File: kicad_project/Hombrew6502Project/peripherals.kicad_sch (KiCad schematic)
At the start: 15 parts, among them J401 SD CARD, J402 Micro_SD_Card, U401 74HCT125D, U402 M95512-Axxx-MF

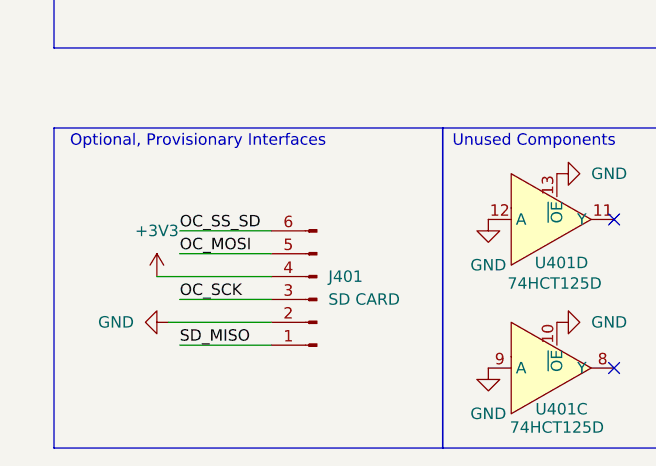
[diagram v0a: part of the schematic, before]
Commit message: footprint assignments and separate project for RAM board
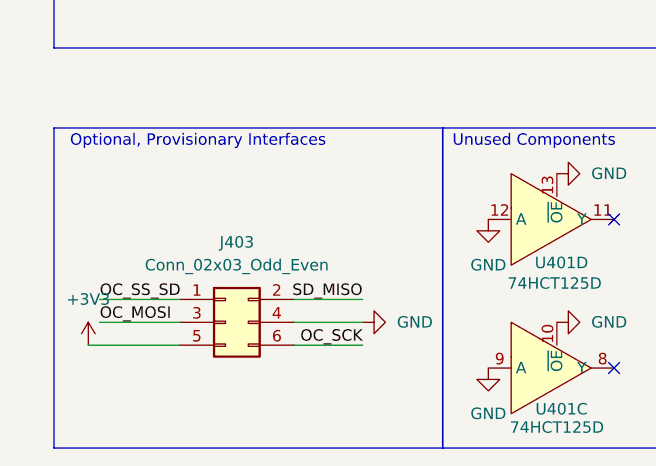
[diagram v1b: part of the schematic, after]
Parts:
- removed J401: SD CARD, symbol Connector:Conn_01x06_Pin
- added J403: Conn_02x03_Odd_Even, Connector_PinHeader_2.54mm:PinHeader_2x03_P2.54mm_Vertical_SMD, symbol Connector_Generic:Conn_02x03_Odd_Even
- J402: footprint (none) -> Connector_Card:microSD_HC_Wuerth_693072010801
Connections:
- net +3V3: now also J403.5 (Pin_5)
- net GND: now also J403.4 (Pin_4)
- net OC_MOSI: now also J403.3 (Pin_3)
- net OC_SCK: now also J403.6 (Pin_6)
- net OC_SS_SD: now also J403.1 (Pin_1)
- net SD_MISO: now also J403.2 (Pin_2)
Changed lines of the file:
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@@
 	(wire
 		(pts
-			(xy 35.56 173.99) (xy 45.72 173.99)
+			(xy 55.88 179.07) (xy 48.26 179.07)
 		)
 		(stroke
@@
 	(wire
 		(pts
-			(xy 33.02 171.45) (xy 45.72 171.45)
+			(xy 25.4 179.07) (xy 35.56 179.07)
 		)
 		(stroke
@@
 	(wire
 		(pts
-			(xy 34.29 176.53) (xy 45.72 176.53)
+			(xy 55.88 176.53) (xy 48.26 176.53)
 		)
 		(stroke
@@
 	(wire
 		(pts
-			(xy 35.56 166.37) (xy 45.72 166.37)
+			(xy 26.67 173.99) (xy 35.56 173.99)
 		)
 		(stroke
@@
 	(wire
 		(pts
-			(xy 35.56 179.07) (xy 45.72 179.07)
+			(xy 55.88 173.99) (xy 48.26 173.99)
 		)
 		(stroke
@@
 	(wire
 		(pts
-			(xy 35.56 168.91) (xy 45.72 168.91)
+			(xy 26.67 176.53) (xy 35.56 176.53)
 		)
 		(stroke
@@
 	)
 	(label "OC_SCK"
-		(at 35.56 173.99 0)
+		(at 55.88 179.07 180)
 		(effects
 			(font
 				(size 1.27 1.27)
 			)
-			(justify left bottom)
+			(justify right bottom)
 		)
 	)
 	(label "SD_MISO"
-		(at 35.56 179.07 0)
+		(at 55.88 173.99 180)
 		(effects
 			(font
 				(size 1.27 1.27)
 			)
-			(justify left bottom)
+			(justify right bottom)
 		)
 	)
@@
 	)
 	(label "OC_MOSI"
-		(at 35.56 168.91 0)
+		(at 26.67 176.53 0)
 		(effects
 			(font
@@
 	)
 	(label "OC_SS_SD"
-		(at 35.56 166.37 0)
+		(at 26.67 173.99 0)
 		(effects
 			(font
@@
 	(symbol
 		(lib_id "power:+3V3")
-		(at 33.02 171.45 0)
+		(at 25.4 179.07 0)
 		(unit 1)
 		(exclude_from_sim no)
@@
 		(fields_autoplaced yes)
 		(property "Reference" "#PWR0419"
-			(at 33.02 175.26 0)
+			(at 25.4 182.88 0)
 			(effects
 				(font
@@
 		)
 		(property "Value" "+3V3"
-			(at 33.02 166.37 0)
+			(at 25.4 173.99 0)
 			(effects
 				(font
@@
 		)
 		(property "Footprint" ""
-			(at 33.02 171.45 0)
+			(at 25.4 179.07 0)
 			(effects
 				(font
@@
 		)
 		(property "Datasheet" ""
-			(at 33.02 171.45 0)
+			(at 25.4 179.07 0)
 			(effects
 				(font
@@
 		)
 		(property "Description" "Power symbol creates a global label with name \"+3V3\""
-			(at 33.02 171.45 0)
+			(at 25.4 179.07 0)
 			(effects
 				(font
@@
 	)
 	(symbol
-		(lib_id "Connector:Conn_01x06_Pin")
-		(at 50.8 173.99 180)
-		(unit 1)
-		(exclude_from_sim no)
-		(in_bom yes)
-		(on_board yes)
-		(dnp no)
-		(fields_autoplaced yes)
-		(property "Reference" "J401"
-			(at 52.07 171.4499 0)
-			(effects
-				(font
-					(size 1.27 1.27)
-				)
-				(justify right)
-			)
-		)
-		(property "Value" "SD CARD"
-			(at 52.07 173.9899 0)
-			(effects
-				(font
-					(size 1.27 1.27)
-				)
-				(justify right)
-			)
-		)
-		(property "Footprint" ""
-			(at 50.8 173.99 0)
-			(effects
-				(font
-					(size 1.27 1.27)
-				)
-				(hide yes)
-			)
-		)
-		(property "Datasheet" "~"
-			(at 50.8 173.99 0)
-			(effects
-				(font
-					(size 1.27 1.27)
-				)
-				(hide yes)
-			)
-		)
-		(property "Description" "Generic connector, single row, 01x06, script generated"
-			(at 50.8 173.99 0)
-			(effects
-				(font
-					(size 1.27 1.27)
-				)
-				(hide yes)
-			)
-		)
-		(property "t_pd (ns)" ""
-			(at 50.8 173.99 0)
-			(effects
-				(font
-					(size 1.27 1.27)
-				)
-				(hide yes)
-			)
-		)
-		(pin "6"
-		)
-		(pin "4"
-		)
-		(pin "3"
-		)
-		(pin "2"
-		)
-		(pin "5"
-		)
-		(pin "1"
-		)
-		(instances
-			(project "6502sbc"
-				(path "/dc8636f6-e59e-4c75-ae27-408ad57a23de/5a0be038-7c3c-4556-9482-35a902da59e6/08b45c3e-da15-47b3-b216-096ca0863706/b32c557a-c41b-41ef-922f-df196eff122f"
-					(reference "J401")
-					(unit 1)
-				)
-			)
-		)
-	)
-	(symbol
 		(lib_id "Connector:Micro_SD_Card")
 		(at 135.89 123.19 0)
@@
 			)
 		)
-		(property "Footprint" ""
+		(property "Footprint" "Connector_Card:microSD_HC_Wuerth_693072010801"
 			(at 165.1 115.57 0)
 			(effects
@@
 	)
 	(symbol
+		(lib_id "Connector_Generic:Conn_02x03_Odd_Even")
+		(at 40.64 176.53 0)
+		(unit 1)
+		(exclude_from_sim no)
+		(in_bom yes)
+		(on_board yes)
+		(dnp no)
+		(fields_autoplaced yes)
+		(property "Reference" "J403"
+			(at 41.91 167.64 0)
+			(effects
+				(font
+					(size 1.27 1.27)
+				)
+			)
+		)
+		(property "Value" "Conn_02x03_Odd_Even"
+			(at 41.91 170.18 0)
+			(effects
+				(font
+					(size 1.27 1.27)
+				)
+			)
+		)
+		(property "Footprint" "Connector_PinHeader_2.54mm:PinHeader_2x03_P2.54mm_Vertical_SMD"
+			(at 40.64 176.53 0)
+			(effects
+				(font
+					(size 1.27 1.27)
+				)
+				(hide yes)
+			)
+		)
+		(property "Datasheet" "~"
+			(at 40.64 176.53 0)
+			(effects
+				(font
+					(size 1.27 1.27)
+				)
+				(hide yes)
+			)
+		)
+		(property "Description" "Generic connector, double row, 02x03, odd/even pin numbering scheme (row 1 odd numbers, row 2 even numbers), script generated (kicad-library-utils/schlib/autogen/connector/)"
+			(at 40.64 176.53 0)
+			(effects
+				(font
+					(size 1.27 1.27)
+				)
+				(hide yes)
+			)
+		)
+		(pin "5"
+		)
+		(pin "3"
+		)
+		(pin "1"
+		)
+		(pin "2"
+		)
+		(pin "6"
+		)
+		(pin "4"
+		)
+		(instances
+			(project ""
+				(path "/dc8636f6-e59e-4c75-ae27-408ad57a23de/5a0be038-7c3c-4556-9482-35a902da59e6/08b45c3e-da15-47b3-b216-096ca0863706/b32c557a-c41b-41ef-922f-df196eff122f"
+					(reference "J403")
+					(unit 1)
+				)
+			)
+		)
+	)
+	(symbol
 		(lib_id "power:GND")
 		(at 77.47 176.53 90)
@@
 	(symbol
 		(lib_id "power:GND")
-		(at 34.29 176.53 270)
+		(at 55.88 176.53 90)
 		(unit 1)
 		(exclude_from_sim no)
@@
 		(fields_autoplaced yes)
 		(property "Reference" "#PWR0404"
-			(at 27.94 176.53 0)
+			(at 62.23 176.53 0)
 			(effects
 				(font
@@
 		)
 		(property "Value" "GND"
-			(at 30.48 176.5299 90)
+			(at 59.69 176.5301 90)
 			(effects
 				(font
@@
 		)
 		(property "Footprint" ""
-			(at 34.29 176.53 0)
+			(at 55.88 176.53 0)
 			(effects
 				(font
@@
 		)
 		(property "Datasheet" ""
-			(at 34.29 176.53 0)
+			(at 55.88 176.53 0)
 			(effects
 				(font
@@
 		)
 		(property "Description" "Power symbol creates a global label with name \"GND\" , ground"
-			(at 34.29 176.53 0)
+			(at 55.88 176.53 0)
 			(effects
 				(font
